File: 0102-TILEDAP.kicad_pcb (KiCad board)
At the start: 4 copper layers, 42.1 x 24.6 mm, 49 parts, among them J1 USB-C, J2 IF, J3 TGT, Q1 S8550, SW1 SW_Push, U1 SPX3819M5-L-3-3, U2 STM32F103TBU6, Y1 8MHz

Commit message: Fix USB_ENUM
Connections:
- Q1 pad 1: +3V3 -> Net-(Q1-Pad1)
- Q1 pad 2: Net-(Q1-Pad2) -> +3V3
- R14 pad 2: Net-(Q1-Pad2) -> Net-(Q1-Pad1)
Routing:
- net Net-(Q1-Pad2): track 3.80 -> 0.00 mm
- net Net-(Q1-Pad1): track 0.00 -> 2.51 mm
- net GND: vias 90 -> 89
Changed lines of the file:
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@@
   (net 25 "Net-(R9-Pad2)")
   (net 26 "Net-(D3-Pad1)")
-  (net 27 "Net-(Q1-Pad2)")
+  (net 27 "Net-(Q1-Pad1)")
   (net 28 "/USB_ENUM")
   (net 29 "/LED_CON_BLUE")
@@
     (fp_line (start -0.65 -1.125) (end -0.325 -1.45) (layer "F.Fab") (width 0.1))
     (pad "1" smd roundrect (at -0.9375 -0.95 180) (size 1.475 0.6) (layers "F.Cu" "F.Paste" "F.Mask") (roundrect_rratio 0.25)
-      (net 4 "+3V3") (pinfunction "E") (pintype "passive"))
+      (net 27 "Net-(Q1-Pad1)") (pinfunction "B") (pintype "input"))
     (pad "2" smd roundrect (at -0.9375 0.95 180) (size 1.475 0.6) (layers "F.Cu" "F.Paste" "F.Mask") (roundrect_rratio 0.25)
-      (net 27 "Net-(Q1-Pad2)") (pinfunction "B") (pintype "input"))
+      (net 4 "+3V3") (pinfunction "E") (pintype "passive"))
     (pad "3" smd roundrect (at 0.9375 0 180) (size 1.475 0.6) (layers "F.Cu" "F.Paste" "F.Mask") (roundrect_rratio 0.25)
       (net 31 "Net-(Q1-Pad3)") (pinfunction "C") (pintype "passive"))
@@
       (net 28 "/USB_ENUM") (pintype "passive"))
     (pad "2" smd roundrect (at 0.51 0 180) (size 0.54 0.64) (layers "F.Cu" "F.Paste" "F.Mask") (roundrect_rratio 0.25)
-      (net 27 "Net-(Q1-Pad2)") (pintype "passive"))
+      (net 27 "Net-(Q1-Pad1)") (pintype "passive"))
     (model "${KICAD6_3DMODEL_DIR}/Resistor_SMD.3dshapes/R_0402_1005Metric.step"
       (offset (xyz 0 0 0))
@@
   (segment (start 117.25 103.75) (end 117.25 106.080344) (width 0.25) (layer "F.Cu") (net 2))
   (via (at 114 112.25) (size 0.5) (drill 0.3) (layers "F.Cu" "B.Cu") (net 2))
-  (via (at 114.75 107.5) (size 0.5) (drill 0.3) (layers "F.Cu" "B.Cu") (net 2))
   (via (at 113.25 112.25) (size 0.5) (drill 0.3) (layers "F.Cu" "B.Cu") (net 2))
   (via (at 132.5 119) (size 0.5) (drill 0.3) (layers "F.Cu" "B.Cu") (net 2))
@@
   (segment (start 122 105.5) (end 123 105.5) (width 0.25) (layer "F.Cu") (net 4))
   (segment (start 116.5 105.5) (end 115.6 105.5) (width 0.25) (layer "F.Cu") (net 4))
-  (segment (start 114.1875 105.7125) (end 114.4 105.5) (width 0.2) (layer "F.Cu") (net 4))
+  (segment (start 114.1875 104.9375) (end 114.75 105.5) (width 0.2) (layer "F.Cu") (net 4))
   (segment (start 109.05 107.3) (end 109.2 107.15) (width 0.5) (layer "F.Cu") (net 4))
+  (segment (start 114.1875 104.3) (end 114.1875 104.9375) (width 0.2) (layer "F.Cu") (net 4))
   (segment (start 113.75 113) (end 115.8 113) (width 0.25) (layer "F.Cu") (net 4))
-  (segment (start 114.1875 106.2) (end 114.1875 105.7125) (width 0.2) (layer "F.Cu") (net 4))
+  (segment (start 114.75 105.5) (end 115.6 105.5) (width 0.2) (layer "F.Cu") (net 4))
   (segment (start 125.5 113.75) (end 124.52 113.75) (width 0.2) (layer "F.Cu") (net 4))
-  (segment (start 114.4 105.5) (end 115.6 105.5) (width 0.2) (layer "F.Cu") (net 4))
   (segment (start 124.52 107.75) (end 124.52 106.88) (width 0.2) (layer "F.Cu") (net 4))
   (segment (start 109.05 108.8625) (end 109.05 107.3) (width 0.5) (layer "F.Cu") (net 4))
@@
   (segment (start 121.8375 110.5) (end 123.499999 110.5) (width 0.2) (layer "F.Cu") (net 25))
   (segment (start 120 104.48) (end 120 103.325) (width 0.2) (layer "F.Cu") (net 26))
-  (segment (start 112.74 106.26) (end 114.1875 104.8125) (width 0.2) (layer "F.Cu") (net 27))
-  (segment (start 112.74 107.5) (end 112.74 106.26) (width 0.2) (layer "F.Cu") (net 27))
-  (segment (start 114.1875 104.3) (end 114.1875 104.8125) (width 0.2) (layer "F.Cu") (net 27))
-  (segment (start 113.76 107.5) (end 114.76 108.5) (width 0.2) (layer "F.Cu") (net 28))
-  (segment (start 114.76 108.5) (end 116.1625 108.5) (width 0.2) (layer "F.Cu") (net 28))
+  (segment (start 113.15 106.2) (end 112.74 106.61) (width 0.2) (layer "F.Cu") (net 27))
+  (segment (start 114.1875 106.2) (end 113.15 106.2) (width 0.2) (layer "F.Cu") (net 27))
+  (segment (start 112.74 106.61) (end 112.74 107.5) (width 0.2) (layer "F.Cu") (net 27))
+  (segment (start 113.76 107.5) (end 114.3 107.5) (width 0.2) (layer "F.Cu") (net 28))
+  (segment (start 114.3 107.5) (end 115.3 108.5) (width 0.2) (layer "F.Cu") (net 28))
+  (segment (start 115.3 108.5) (end 116.1625 108.5) (width 0.2) (layer "F.Cu") (net 28))
   (segment (start 120.5 107.1625) (end 120.5 106) (width 0.2) (layer "F.Cu") (net 29))
   (segment (start 120.5 106) (end 121 105.5) (width 0.2) (layer "F.Cu") (net 29))

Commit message: Update resistor for LED_CON_BLUE
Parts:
- R11: value 1.5K -> 220R
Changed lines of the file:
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@@
     (tags "resistor")
     (property "Manufacturer" "UniOhm")
-    (property "PartNumber" "C25867")
+    (property "PartNumber" "C25091")
     (property "Sheetfile" "0102-TILEDAP.kicad_sch")
     (property "Sheetname" "")
@@
       (effects (font (size 1 1) (thickness 0.15)))
     )
-    (fp_text value "1.5K" (at 0 1.17 90) (layer "F.Fab")
+    (fp_text value "220R" (at 0 1.17 90) (layer "F.Fab")
       (effects (font (size 1 1) (thickness 0.15)))
     )

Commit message: MFDoc V1.3
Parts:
- removed kibuzzard-631EEA50: G***, kibuzzard-631EEA50
- added kibuzzard-63202282: G***, kibuzzard-63202282, F.Cu at (102.5, 118.5)

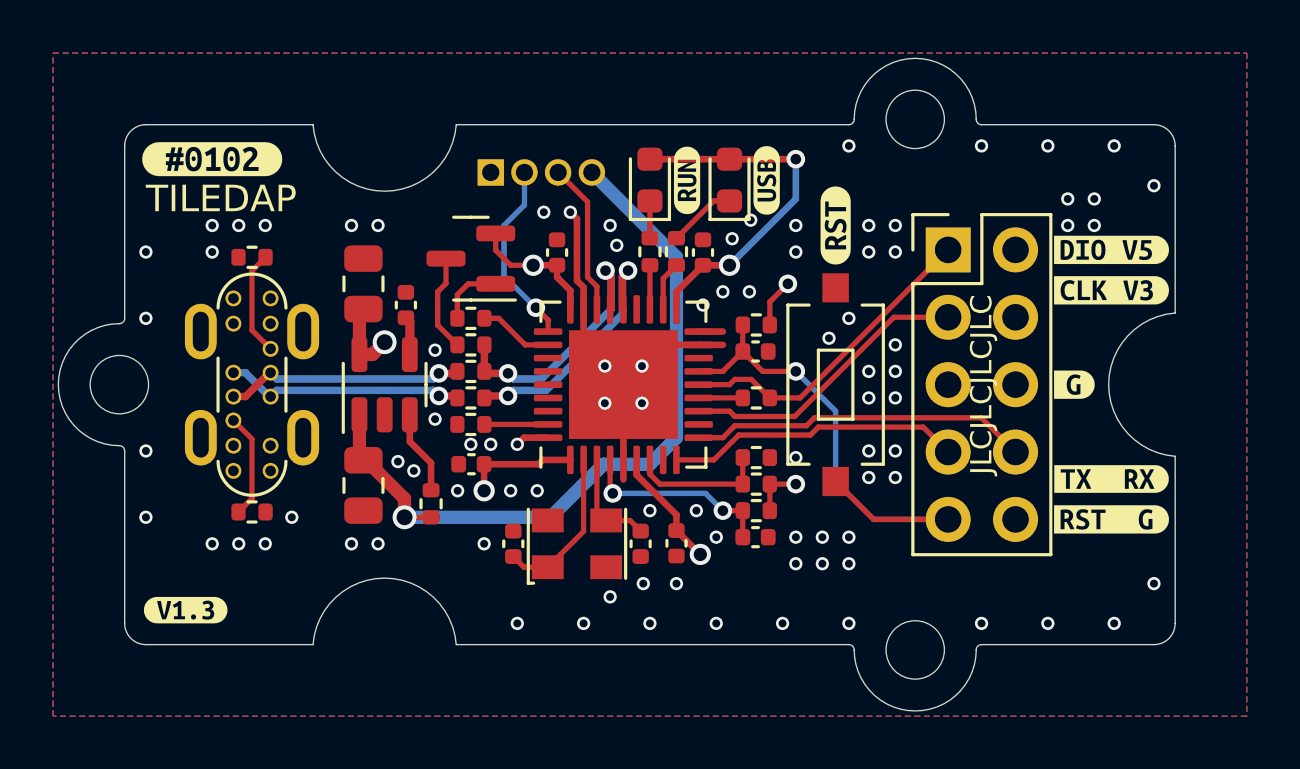
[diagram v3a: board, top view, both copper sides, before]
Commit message: Rework PCB
* Use New boundary
* Use laid USB-C connector
* Add ESDs
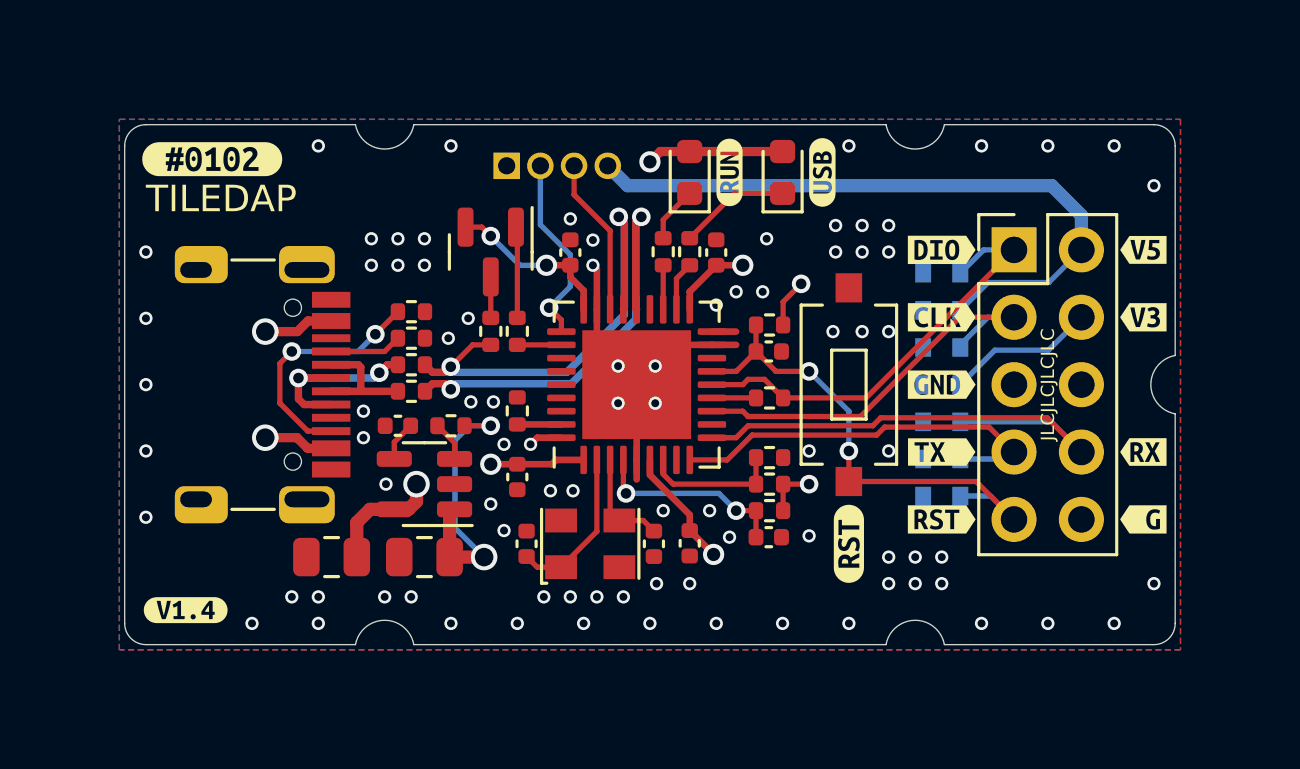
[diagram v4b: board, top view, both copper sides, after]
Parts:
- removed H1, H2, H3: MountingHole, MountingHole:MountingHole_2.2mm_M2
- removed kibuzzard-631DCF04: G***, kibuzzard-631DCF04
- removed kibuzzard-631DCF09: G***, kibuzzard-631DCF09
- removed kibuzzard-631DCF21: G***, kibuzzard-631DCF21
- removed kibuzzard-631DCF2A: G***, kibuzzard-631DCF2A
- removed kibuzzard-631DCF4E: G***, kibuzzard-631DCF4E
- removed kibuzzard-63202282: G***, kibuzzard-63202282
- added D7: LESD5Z5.0CT1G, Diode_SMD:D_SOD-523, B.Cu at (131.0, 111.4)
- added D?: LESD5Z5.0CT1G, Diode_SMD:D_SOD-523, B.Cu at (131.0, 114.2)
- added D?: LESD5Z5.0CT1G, Diode_SMD:D_SOD-523, B.Cu at (131.0, 108.6)
- added D?: LESD5Z5.0CT1G, Diode_SMD:D_SOD-523, B.Cu at (131.0, 107.2)
- added D?: LESD5Z5.0CT1G, Diode_SMD:D_SOD-523, B.Cu at (131.0, 110.0)
- added D?: LESD5Z5.0CT1G, Diode_SMD:D_SOD-523, B.Cu at (131.0, 112.8)
- added D?: LESD5Z5.0CT1G, Diode_SMD:D_SOD-523, B.Cu at (131.0, 105.8)
- added kibuzzard-6329514A: G***, kibuzzard-6329514A, F.Cu at (138.6, 104.9)
- added kibuzzard-63295172: G***, kibuzzard-63295172, F.Cu at (138.6, 107.5)
- added kibuzzard-63295177: G***, kibuzzard-63295177, F.Cu at (138.6, 112.5)
- added kibuzzard-63295187: G***, kibuzzard-63295187, F.Cu at (138.6, 115.1)
- added kibuzzard-632952D1: G***, kibuzzard-632952D1, F.Cu at (131.0, 104.9)
- added kibuzzard-632952D9: G***, kibuzzard-632952D9, F.Cu at (131.0, 107.5)
- added kibuzzard-632952DE: G***, kibuzzard-632952DE, F.Cu at (131.0, 110.0)
- added kibuzzard-632952E3: G***, kibuzzard-632952E3, F.Cu at (131.0, 112.5)
- added kibuzzard-632952EA: G***, kibuzzard-632952EA, F.Cu at (131.0, 115.1)
- added kibuzzard-632A8CA6: G***, kibuzzard-632A8CA6, F.Cu at (102.5, 118.5)
- J1: footprint JLC-SMT:KINGHELM_KH-TYPE-C-L10-14P -> JLC-SMT:HRO_TYPE-C-31-M-12
- moved kibuzzard-631DD701 12.0 mm to (127.5, 116.0)
- moved C3 10.4 mm to (108.0, 116.5), turned to 0 degrees
- moved R3 9.65 mm to (111.0, 107.2)
- moved R1 6.74 mm to (111.0, 108.2), turned to 180 degrees
- moved C2 4.56 mm to (110.5, 111.5), turned to 0 degrees
- moved U1 4.04 mm to (111.5, 113.8), turned to 180 degrees
- moved C1 3.55 mm to (111.5, 116.5), turned to 0 degrees
- moved R2 3.03 mm to (112.5, 111.5), turned to 0 degrees
- moved J3 2.48 mm to (133.7, 104.9)
- moved R4 2.25 mm to (111.0, 110.2)
- moved R5 2.25 mm to (111.0, 109.2)
- moved kibuzzard-631DD70B 2.12 mm to (126.5, 102.0)
- moved D1 2.02 mm to (125.0, 102.0)
- moved R8 1.82 mm to (115.0, 111.0), turned to 90 degrees
- moved R14 1.82 mm to (115.0, 108.0), turned to 90 degrees
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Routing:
- net VBUS: track 48.5 -> 75.0 mm, vias 1 -> 4
- net +3V3: track 82.3 -> 93.8 mm, vias 8 -> 9
- net /TGT_USB_D+: track 10.1 -> 17.9 mm
- net /TGT_RX: track 12.8 -> 19.8 mm
- net /TGT_USB_D-: track 9.80 -> 16.8 mm
- net Net-(J1-PadB5): track 3.95 -> 9.13 mm, vias 0 -> 2
- net /D-: track 9.03 -> 4.58 mm, vias 1 -> 0
- net /TGT_SWCLK: track 11.0 -> 15.5 mm
- net /TGT_SWDIO: track 12.1 -> 16.5 mm
- net /TGT_TX: track 11.1 -> 15.3 mm
- net GND: track 17.5 -> 15.3 mm, vias 89 -> 86
- net Net-(Q1-Pad3): track 3.69 -> 1.54 mm
- net /D+: track 9.03 -> 7.30 mm, vias 1 -> 2
- net Net-(R2-Pad1): track 3.17 -> 1.52 mm
- net Net-(D1-Pad1): track 2.58 -> 4.20 mm
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- removed copper zone on In2.Cu, net VBUS
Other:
- board size 42.1 x 24.6 mm -> 39.6 x 19.6 mm
- board text added: "VBUS SWDIO SWCLK GND"
- board text removed: "5V"
- board text removed: "GND"
- board text removed: "SWCK"
- board text removed: "SWIO"
